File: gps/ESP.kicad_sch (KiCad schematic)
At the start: 7 parts, among them J6 Conn_01x04, J7 USB_B_Micro, J8 Conn_01x04, SW1 RotaryEncoder_Switch, U3 DFR0654

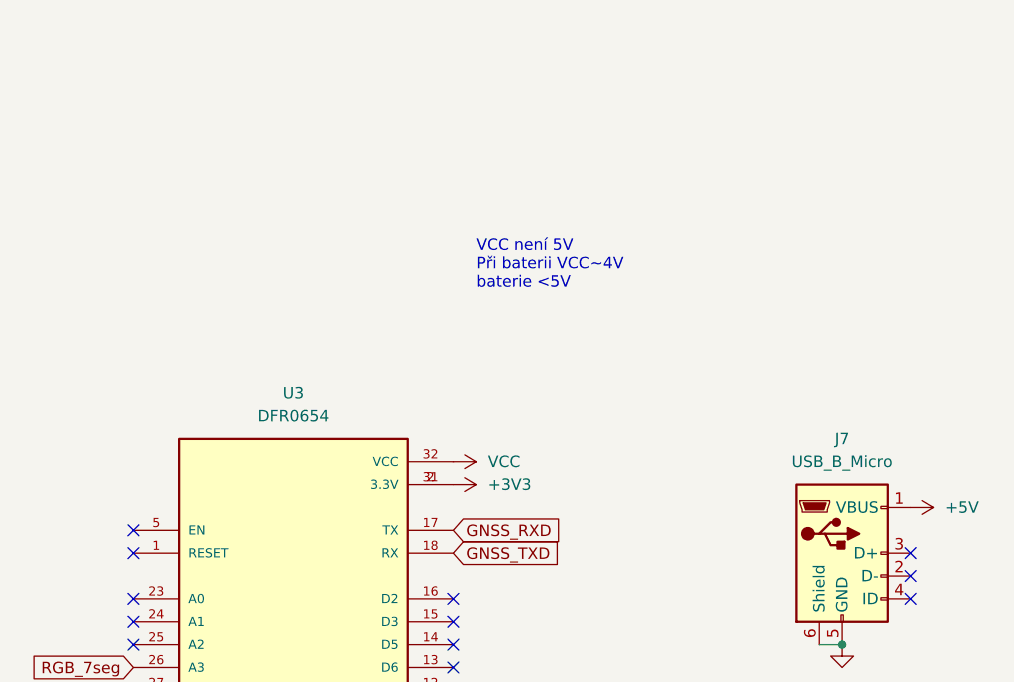
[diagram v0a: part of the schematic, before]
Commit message: update pcd/sch
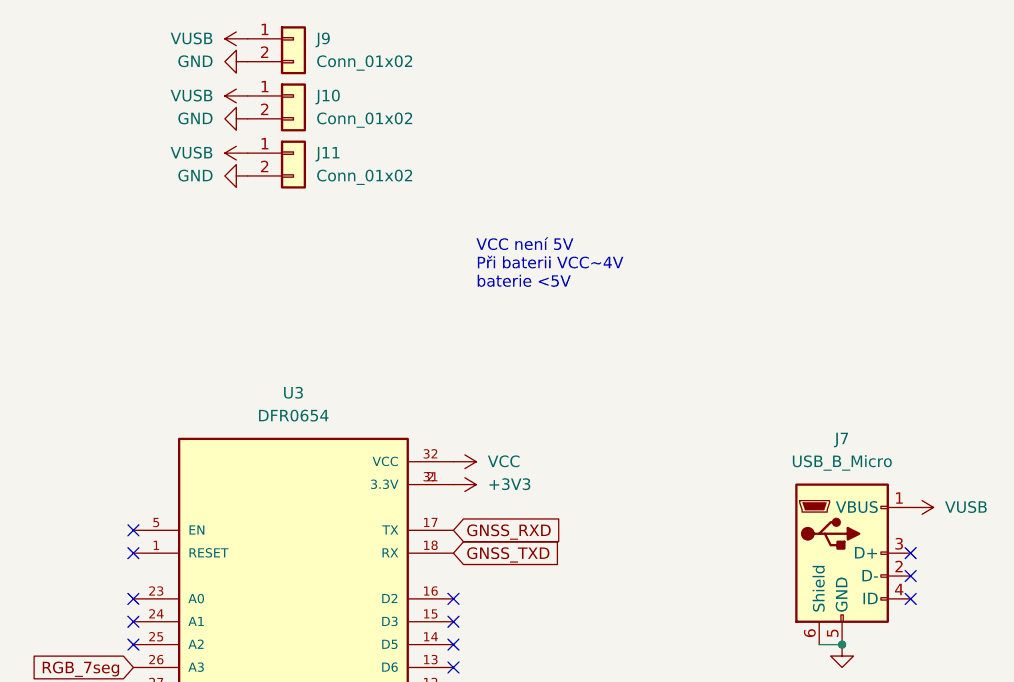
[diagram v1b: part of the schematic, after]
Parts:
- added J10: Conn_01x02, Connector_PinHeader_2.54mm:PinHeader_1x02_P2.54mm_Vertical, symbol Connector_Generic:Conn_01x02
- added J11, J9: Conn_01x02, Connector_PinSocket_2.54mm:PinSocket_1x02_P2.54mm_Vertical, symbol Connector_Generic:Conn_01x02
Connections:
- net GND: now also J10.2 (Pin_2), J11.2 (Pin_2), J9.2 (Pin_2)
- net +5V renamed VUSB
- net VUSB: now also J10.1 (Pin_1), J11.1 (Pin_1), J9.1 (Pin_1)

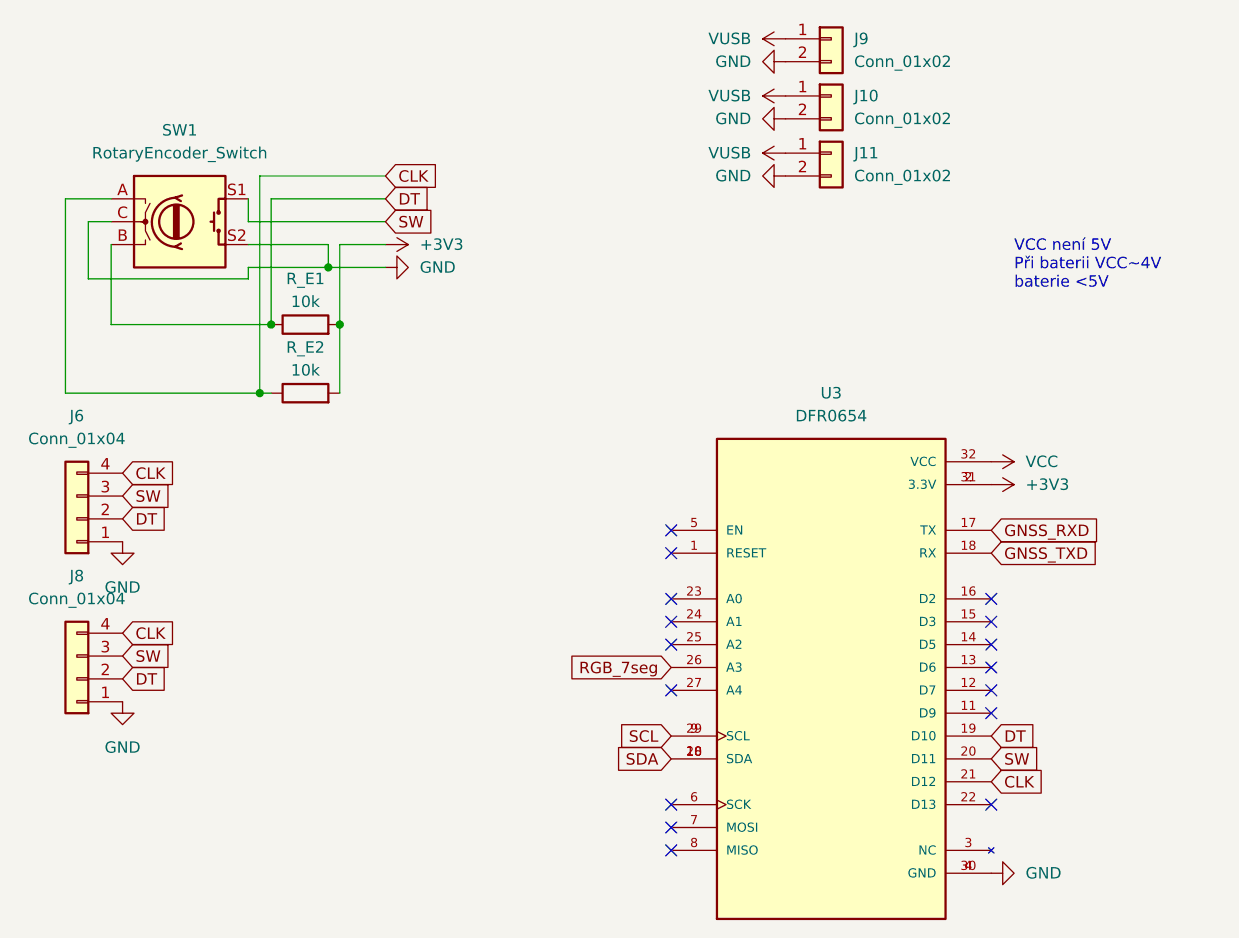
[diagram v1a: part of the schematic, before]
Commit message: update pcd/sch
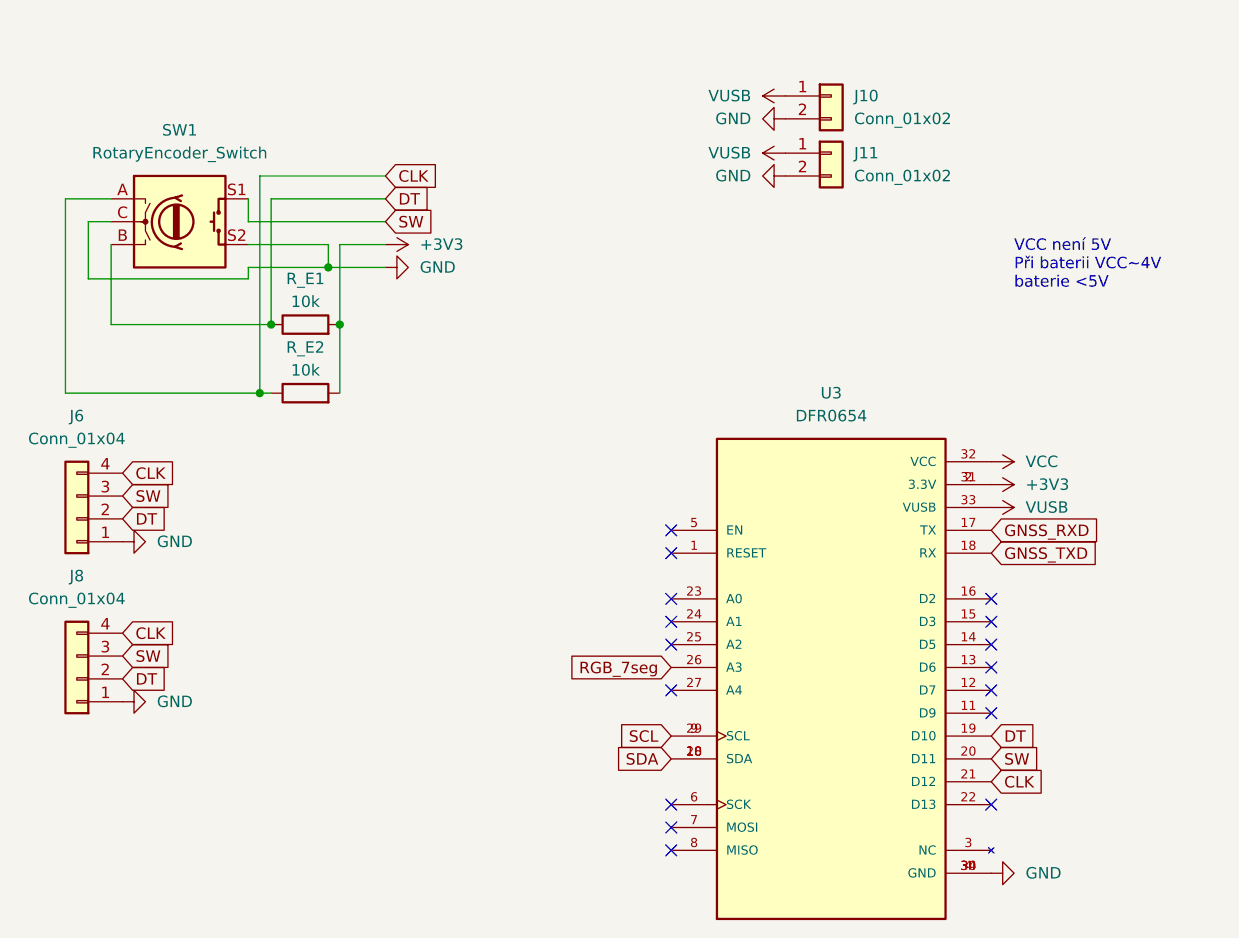
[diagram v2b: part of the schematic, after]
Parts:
- removed J9: Conn_01x02, Connector_PinSocket_2.54mm:PinSocket_1x02_P2.54mm_Vertical, symbol Connector_Generic:Conn_01x02
- U3: Description_1 (none) -> ESP32 ESP32-E Transceiver; 802.11 b/g/n/d/e/i/k/r (Wi-Fi, W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
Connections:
- net GND: now also U3.34 (GND)
- net VUSB: now also U3.33 (VUSB)
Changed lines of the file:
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@@
+	)
+	(symbol
+		(lib_id "power:+5C")
+		(at 138.43 77.47 270)
+		(unit 1)
+		(exclude_from_sim no)
+		(in_bom yes)
+		(on_board yes)
+		(dnp no)
+		(fields_autoplaced yes)
+		(property "Reference" "#PWR01"
+			(at 134.62 77.47 0)
+			(effects
+				(font
+					(size 1.27 1.27)
+				)
+				(hide yes)
+			)
+		)
+		(property "Value" "VUSB"
+			(at 142.24 77.4699 90)
+			(effects
+				(font
+					(size 1.27 1.27)
+				)
+				(justify left)
+			)
+		)
+		(property "Footprint" ""
+			(at 138.43 77.47 0)
+			(effects
+				(font
+					(size 1.27 1.27)
+				)
+				(hide yes)
+			)
+		)
+		(property "Datasheet" ""
+			(at 138.43 77.47 0)
+			(effects
+				(font
+					(size 1.27 1.27)
+				)
+				(hide yes)
+			)
+		)
+		(property "Description" "Power symbol creates a global label with name \"+5C\""
+			(at 138.43 77.47 0)
+			(effects
+				(font
+					(size 1.27 1.27)
+				)
+				(hide yes)
+			)
+		)
+		(pin "1"
+		)
+		(instances
+			(project "gps"
+				(path "/00526ddc-5304-4072-af1e-192a9e7e83da/2d592f67-4c05-4d6d-98b6-6efe4fa6f706"
+					(reference "#PWR01")
+					(unit 1)
+				)
+			)
+		)
 	)
 	(symbol
 		(lib_id "power:GND")
-		(at 115.57 27.94 270)
-		(unit 1)
-		(exclude_from_sim no)
-		(in_bom yes)
-		(on_board yes)
-		(dnp no)
-		(fields_autoplaced yes)
-		(property "Reference" "#PWR046"
-			(at 109.22 27.94 0)
+		(at 41.91 81.28 90)
+		(unit 1)
+		(exclude_from_sim no)
+		(in_bom yes)
+		(on_board yes)
+		(dnp no)
+		(fields_autoplaced yes)
+		(property "Reference" "#PWR032"
+			(at 48.26 81.28 0)
 			(effects
 				(font
@@
 		)
 		(property "Value" "GND"
-			(at 111.76 27.9399 90)
+			(at 45.72 81.2799 90)
 			(effects
 				(font
@@
 				)
 				(justify right)
-			)
-		)
-		(property "Footprint" ""
-			(at 115.57 27.94 0)
-			(effects
-				(font
-					(size 1.27 1.27)
-				)
-				(hide yes)
-			)
-		)
-		(property "Datasheet" ""
-			(at 115.57 27.94 0)
-			(effects
-				(font
-					(size 1.27 1.27)
-				)
-				(hide yes)
-			)
-		)
-		(property "Description" "Power symbol creates a global label with name \"GND\" , ground"
-			(at 115.57 27.94 0)
-			(effects
-				(font
-					(size 1.27 1.27)
-				)
-				(hide yes)
-			)
-		)
-		(pin "1"
-		)
-		(instances
-			(project "gps"
-				(path "/00526ddc-5304-4072-af1e-192a9e7e83da/2d592f67-4c05-4d6d-98b6-6efe4fa6f706"
-					(reference "#PWR046")
-					(unit 1)
-				)
-			)
-		)
-	)
-	(symbol
-		(lib_id "power:+5C")
-		(at 115.57 25.4 90)
-		(unit 1)
-		(exclude_from_sim no)
-		(in_bom yes)
-		(on_board yes)
-		(dnp no)
-		(fields_autoplaced yes)
-		(property "Reference" "#PWR01"
-			(at 119.38 25.4 0)
-			(effects
-				(font
-					(size 1.27 1.27)
-				)
-				(hide yes)
-			)
-		)
-		(property "Value" "VUSB"
-			(at 111.76 25.3999 90)
-			(effects
-				(font
-					(size 1.27 1.27)
-				)
-				(justify left)
-			)
-		)
-		(property "Footprint" ""
-			(at 115.57 25.4 0)
-			(effects
-				(font
-					(size 1.27 1.27)
-				)
-				(hide yes)
-			)
-		)
-		(property "Datasheet" ""
-			(at 115.57 25.4 0)
-			(effects
-				(font
-					(size 1.27 1.27)
-				)
-				(hide yes)
-			)
-		)
-		(property "Description" "Power symbol creates a global label with name \"+5C\""
-			(at 115.57 25.4 0)
-			(effects
-				(font
-					(size 1.27 1.27)
-				)
-				(hide yes)
-			)
-		)
-		(pin "1"
-		)
-		(instances
-			(project ""
-				(path "/00526ddc-5304-4072-af1e-192a9e7e83da/2d592f67-4c05-4d6d-98b6-6efe4fa6f706"
-					(reference "#PWR01")
-					(unit 1)
-				)
-			)
-		)
-	)
-	(symbol
-		(lib_id "power:GND")
-		(at 41.91 81.28 0)
-		(unit 1)
-		(exclude_from_sim no)
-		(in_bom yes)
-		(on_board yes)
-		(dnp no)
-		(fields_autoplaced yes)
-		(property "Reference" "#PWR032"
-			(at 41.91 87.63 0)
-			(effects
-				(font
-					(size 1.27 1.27)
-				)
-				(hide yes)
-			)
-		)
-		(property "Value" "GND"
-			(at 41.91 86.36 0)
-			(effects
-				(font
-					(size 1.27 1.27)
-				)
 			)
 		)
@@
 			)
 		)
+		(property "Description_1" "\nESP32 ESP32-E Transceiver; 802.11 b/g/n/d/e/i/k/r (Wi-Fi, WiFi, WLAN), Bluetooth® Smart 4.x Low Energy (BLE) 2.4GHz ~ 2.5GHz Evaluation Board\n"
+			(at 120.65 95.25 0)
+			(effects
+				(font
+					(size 1.27 1.27)
+				)
+				(justify bottom)
+				(hide yes)
+			)
+		)
 		(pin "1"
 		)
@@
 		)
 		(pin "9"
+		)
+		(pin "33"
+		)
+		(pin "34"
 		)
 		(instances
@@
 	)
 	(symbol
-		(lib_id "Connector_Generic:Conn_01x02")
-		(at 120.65 25.4 0)
-		(unit 1)
-		(exclude_from_sim no)
-		(in_bom yes)
-		(on_board yes)
-		(dnp no)
-		(fields_autoplaced yes)
-		(property "Reference" "J9"
-			(at 123.19 25.3999 0)
-			(effects
-				(font
-					(size 1.27 1.27)
-				)
-				(justify left)
-			)
-		)
-		(property "Value" "Conn_01x02"
-			(at 123.19 27.9399 0)
-			(effects
-				(font
-					(size 1.27 1.27)
-				)
-				(justify left)
-			)
-		)
-		(property "Footprint" "Connector_PinSocket_2.54mm:PinSocket_1x02_P2.54mm_Vertical"
-			(at 120.65 25.4 0)
-			(effects
-				(font
-					(size 1.27 1.27)
-				)
-				(hide yes)
-			)
-		)
-		(property "Datasheet" "~"
-			(at 120.65 25.4 0)
-			(effects
-				(font
-					(size 1.27 1.27)
-				)
-				(hide yes)
-			)
-		)
-		(property "Description" "Generic connector, single row, 01x02, script generated (kicad-library-utils/schlib/autogen/connector/)"
-			(at 120.65 25.4 0)
-			(effects
-				(font
-					(size 1.27 1.27)
-				)
-				(hide yes)
-			)
-		)
-		(pin "1"
-		)
-		(pin "2"
-		)
-		(instances
-			(project ""
-				(path "/00526ddc-5304-4072-af1e-192a9e7e83da/2d592f67-4c05-4d6d-98b6-6efe4fa6f706"
-					(reference "J9")
-					(unit 1)
-				)
-			)
-		)
-	)
-	(symbol
 		(lib_id "power:+5C")
 		(at 115.57 31.75 90)
@@
 	(symbol
 		(lib_id "power:GND")
-		(at 41.91 99.06 0)
+		(at 41.91 99.06 90)
 		(unit 1)
 		(exclude_from_sim no)
@@
 		(fields_autoplaced yes)
 		(property "Reference" "#PWR034"
-			(at 41.91 105.41 0)
+			(at 48.26 99.06 0)
 			(effects
 				(font
@@
 		)
 		(property "Value" "GND"
-			(at 41.91 104.14 0)
-			(effects
-				(font
-					(size 1.27 1.27)
-				)
-			)
-		)
+			(at 45.72 99.0599 90)
+			(effects
+				(font
+					(size 1.27 1.27)
+				)
+				(justify right)
+			)
+		)
